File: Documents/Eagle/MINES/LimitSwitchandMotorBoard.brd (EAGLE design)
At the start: 36.5 x 48.2 mm, 10 parts, among them IC1 ULN2003AN, IC2 ULN2003AN, X10 B5B-XH-2, X11 B2B-XH-2, X12 B2B-XH-2, X13 B2B-XH-2, X14 B2B-XH-2, X15 B2B-XH-2, X9 B5B-XH-2

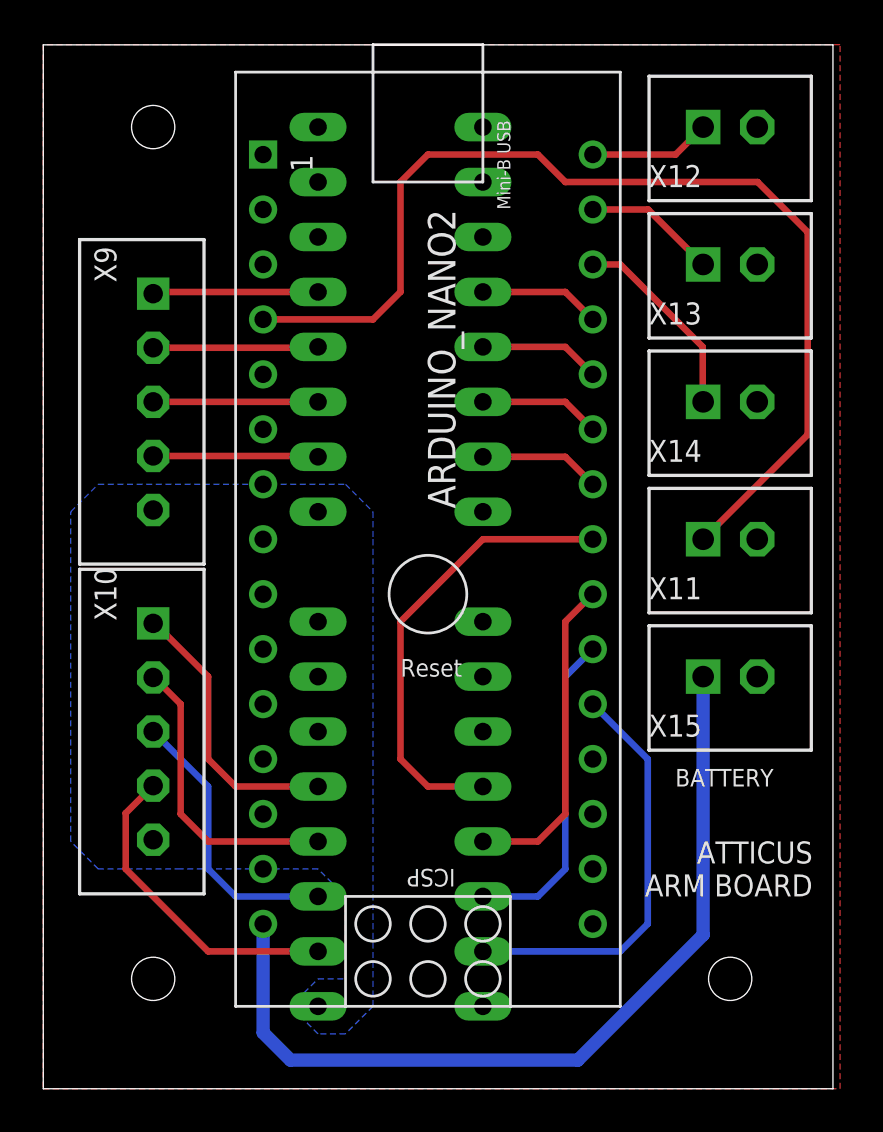
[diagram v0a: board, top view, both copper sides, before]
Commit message: Added 3-head breakouts to both boards and team name
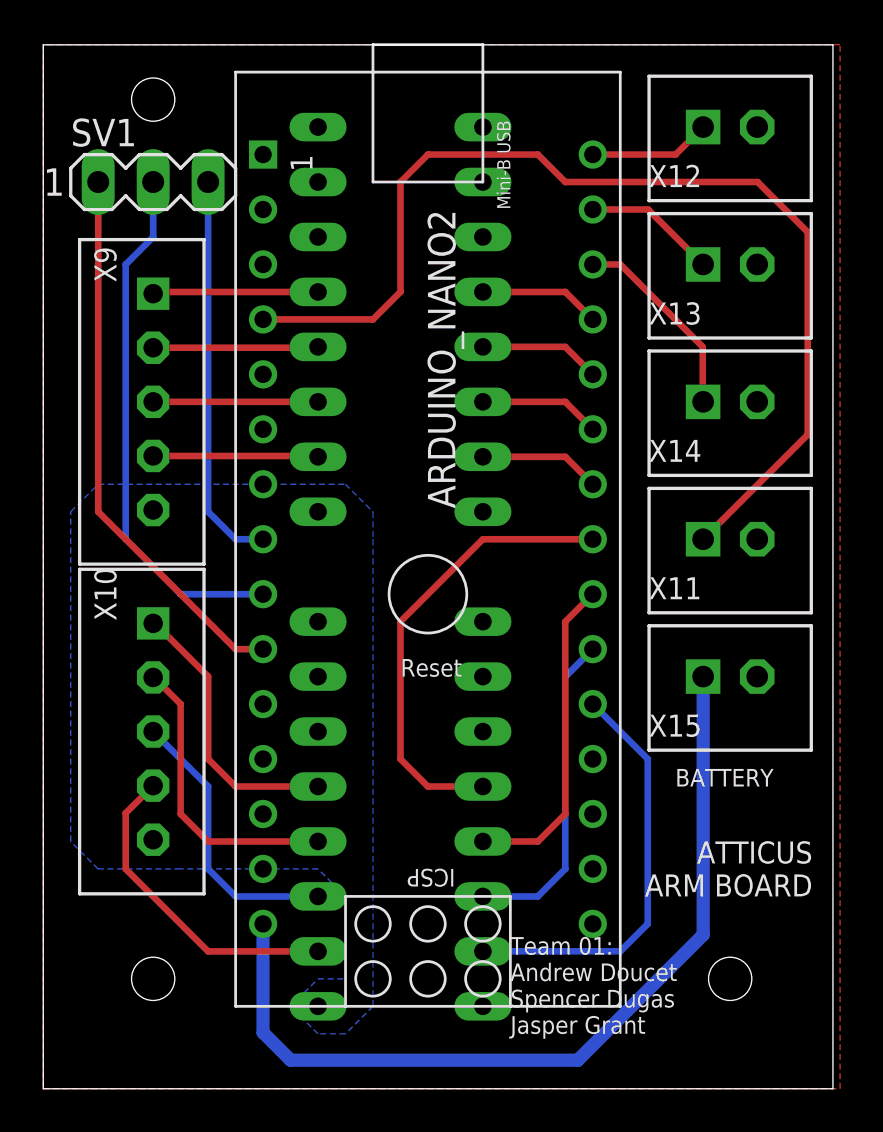
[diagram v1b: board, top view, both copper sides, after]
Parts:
- added SV1: (no value), con-lstb:MA03-1
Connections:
- new net N$20: ARDUINO_NANO2.8, SV1.3
- new net N$21: ARDUINO_NANO2.9, SV1.2
- new net N$22: ARDUINO_NANO2.10, SV1.1
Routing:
- net N$22: track 0.00 -> 25.5 mm
- net N$21: track 0.00 -> 24.4 mm
- net N$20: track 0.00 -> 18.3 mm
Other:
- board text added: "Team 01: Andrew Doucet Spencer Dugas Jasper Grant"
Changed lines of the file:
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@@
 <wire x1="35.23" y1="80" x2="-1.27" y2="80" width="0" layer="20"/>
 <wire x1="-1.27" y1="80" x2="-1.27" y2="31.75" width="0" layer="20"/>
-<hole x="3.81" y="76.2" drill="2"/>
+<hole x="3.81" y="77.47" drill="2"/>
 <hole x="30.48" y="36.83" drill="2"/>
 <hole x="3.81" y="36.83" drill="2"/>
@@
 <text x="34.29" y="43.18" size="1.016" layer="25" rot="R180">ATTICUS
 ARM BOARD</text>
+<text x="20.32" y="34.29" size="0.8128" layer="25">Team 01:
+Andrew Doucet
+Spencer Dugas
+Jasper Grant</text>
 </plain>
 <attributes>
@@
 <attribute name="VALUE" x="29.23" y="49.53" size="1.016" layer="27" rot="R180" align="bottom-right"/>
 </element>
+<element name="SV1" library="con-lstb" library_urn="urn:adsk.eagle:library:162" package="MA03-1" package3d_urn="urn:adsk.eagle:package:8339/1" value="" x="3.81" y="73.66" smashed="yes">
+<attribute name="MF" value="" x="3.81" y="73.66" size="1.778" layer="27" display="off"/>
+<attribute name="MPN" value="" x="3.81" y="73.66" size="1.778" layer="27" display="off"/>
+<attribute name="NAME" x="0" y="75.311" size="1.27" layer="25" ratio="10"/>
+<attribute name="OC_FARNELL" value="unknown" x="3.81" y="73.66" size="1.778" layer="27" display="off"/>
+<attribute name="OC_NEWARK" value="unknown" x="3.81" y="73.66" size="1.778" layer="27" display="off"/>
+<attribute name="POPULARITY" value="48" x="3.81" y="73.66" size="1.778" layer="27" display="off"/>
+<attribute name="VALUE" x="0" y="70.739" size="1.27" layer="27" ratio="10"/>
+</element>
 </elements>
 <signals>
@@
 <wire x1="23.4386875" y1="33.0708" x2="29.23" y2="38.8621125" width="0.6096" layer="16"/>
 </signal>
+<signal name="N$20">
+<contactref element="ARDUINO_NANO2" pad="8"/>
+<contactref element="SV1" pad="3"/>
+<wire x1="8.89" y1="57.15" x2="7.62" y2="57.15" width="0.3048" layer="16"/>
+<wire x1="7.62" y1="57.15" x2="6.35" y2="58.42" width="0.3048" layer="16"/>
+<wire x1="6.35" y1="58.42" x2="6.35" y2="73.66" width="0.3048" layer="16"/>
+</signal>
+<signal name="N$21">
+<contactref element="SV1" pad="2"/>
+<contactref element="ARDUINO_NANO2" pad="9"/>
+<wire x1="8.89" y1="54.61" x2="5.08" y2="54.61" width="0.3048" layer="16"/>
+<wire x1="5.08" y1="54.61" x2="2.54" y2="57.15" width="0.3048" layer="16"/>
+<wire x1="2.54" y1="57.15" x2="2.54" y2="69.85" width="0.3048" layer="16"/>
+<wire x1="2.54" y1="69.85" x2="3.81" y2="71.12" width="0.3048" layer="16"/>
+<wire x1="3.81" y1="71.12" x2="3.81" y2="73.66" width="0.3048" layer="16"/>
+</signal>
+<signal name="N$22">
+<contactref element="ARDUINO_NANO2" pad="10"/>
+<contactref element="SV1" pad="1"/>
+<wire x1="8.89" y1="52.07" x2="7.62" y2="52.07" width="0.3048" layer="1"/>
+<wire x1="7.62" y1="52.07" x2="1.27" y2="58.42" width="0.3048" layer="1"/>
+<wire x1="1.27" y1="58.42" x2="1.27" y2="73.66" width="0.3048" layer="1"/>
+</signal>
 </signals>
